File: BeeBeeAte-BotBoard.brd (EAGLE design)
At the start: 99 x 100 mm, 100 parts, among them IC1 CP2102, J1 3-1734035-2, T1 S8050, T2 S8050, U1 ESP32-WROOM-32, U2 LM5.0, U3 DRIVER 2, U4 DRIVER 1, U5 DRIVER 3, U6 DRIVER 4

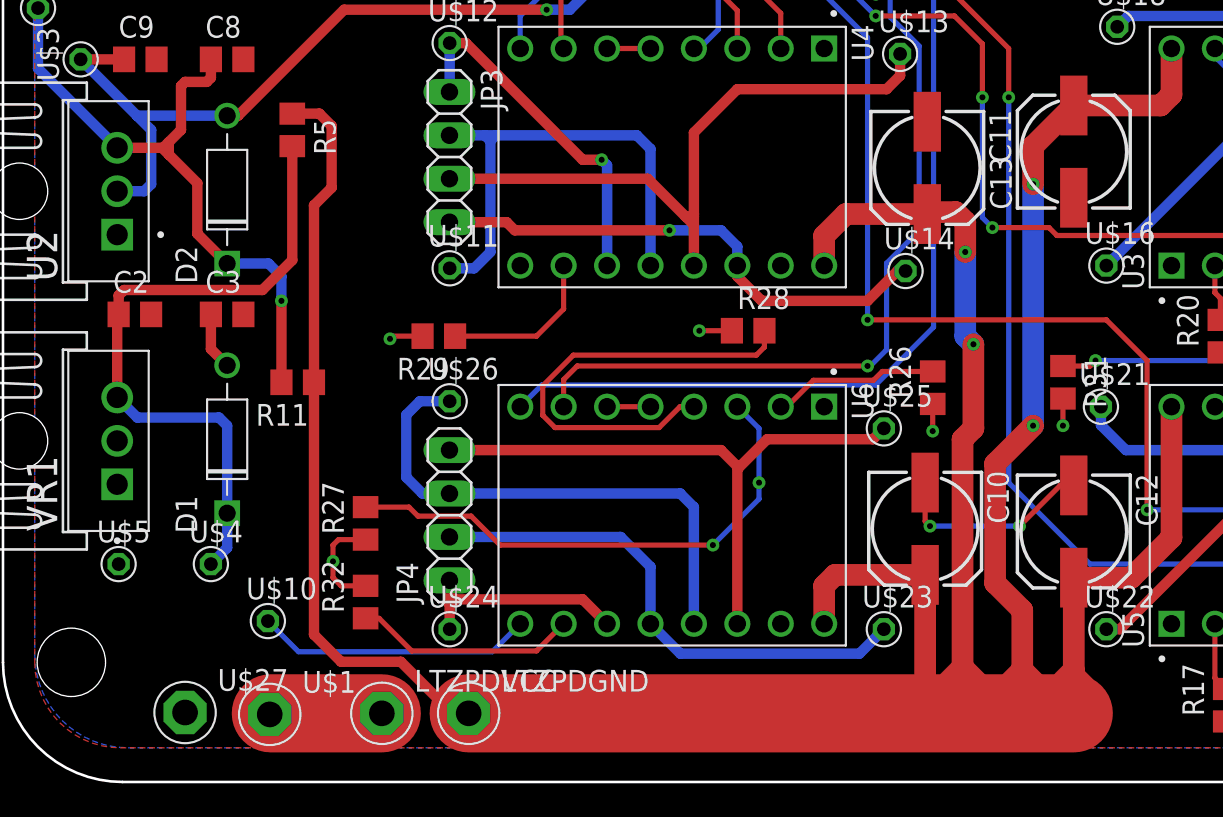
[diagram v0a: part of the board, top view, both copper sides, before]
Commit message: Added 3,7V battery
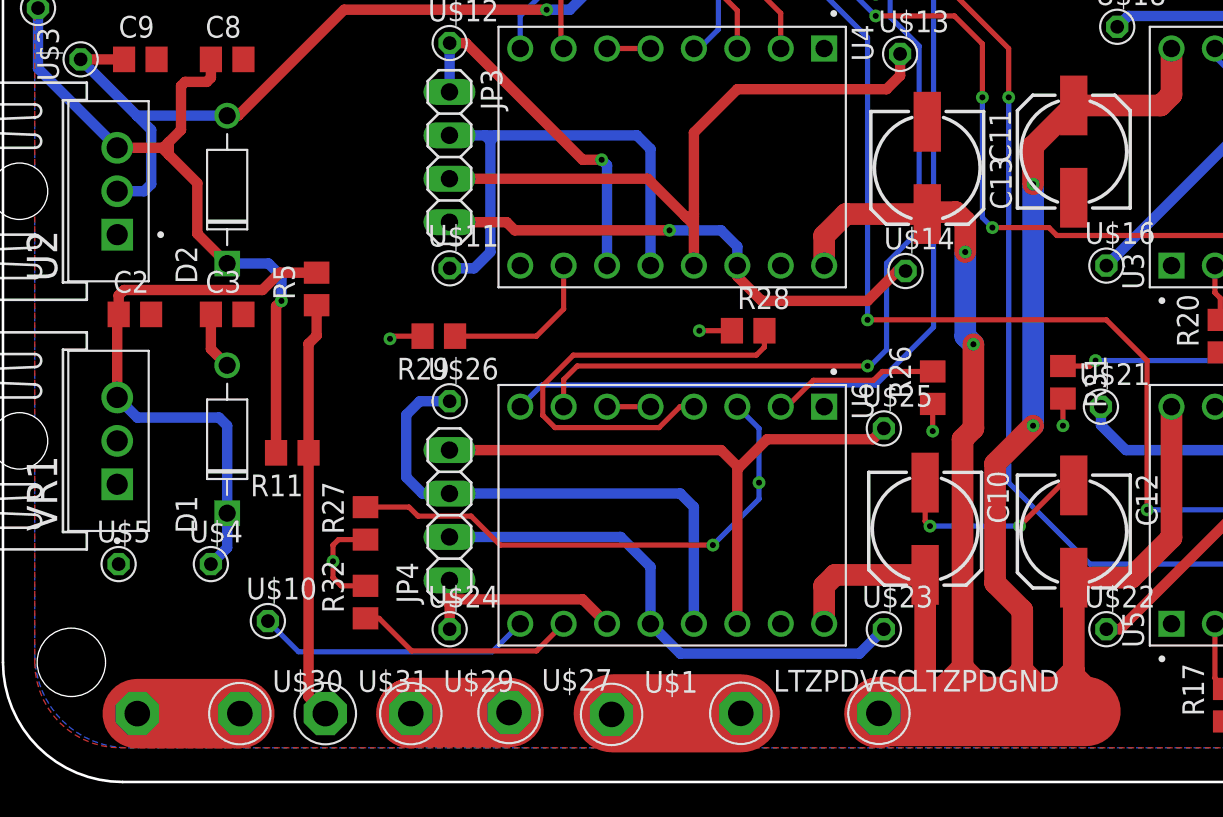
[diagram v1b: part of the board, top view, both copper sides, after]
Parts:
- added U$28: 9V+, 03lanfra-PADS:LITZENPAD
- added U$29: 9V-, 03lanfra-PADS:LITZENPAD
- added U$30: 9VSW+, 03lanfra-PADS:LITZENPAD
- added U$31: 9VSW-, 03lanfra-PADS:LITZENPAD
- moved LTZPDGND 24.0 mm to (51.4, 4.02)
- moved LTZPDVCC 21.0 mm to (43.3, 4.02)
- moved U$1 20.0 mm to (35.7, 3.95)
- moved U$27 19.0 mm to (29.7, 4.07)
- moved R5 9.41 mm to (18.5, 28.8), turned to 90 degrees
- moved R11 4.14 mm to (17.1, 19.3)
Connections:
- new net 9V: R11.1, R5.1, U$31.P$1
- new net N$15: U$28.P$1, U$30.P$1
- net GND: now also U$29.P$1
- net VCC: no longer R11.1, R5.1
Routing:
- net VCC: track 209.4 -> 142.4 mm
- net 9V: track 0.00 -> 24.5 mm
- net N$15: track 0.00 -> 6.00 mm
- net GND: track 121.6 -> 127.3 mm
- net N$4: track 39.3 -> 33.7 mm
- net N$8: track 38.6 -> 42.9 mm
- net N$5: track 6.58 -> 7.58 mm

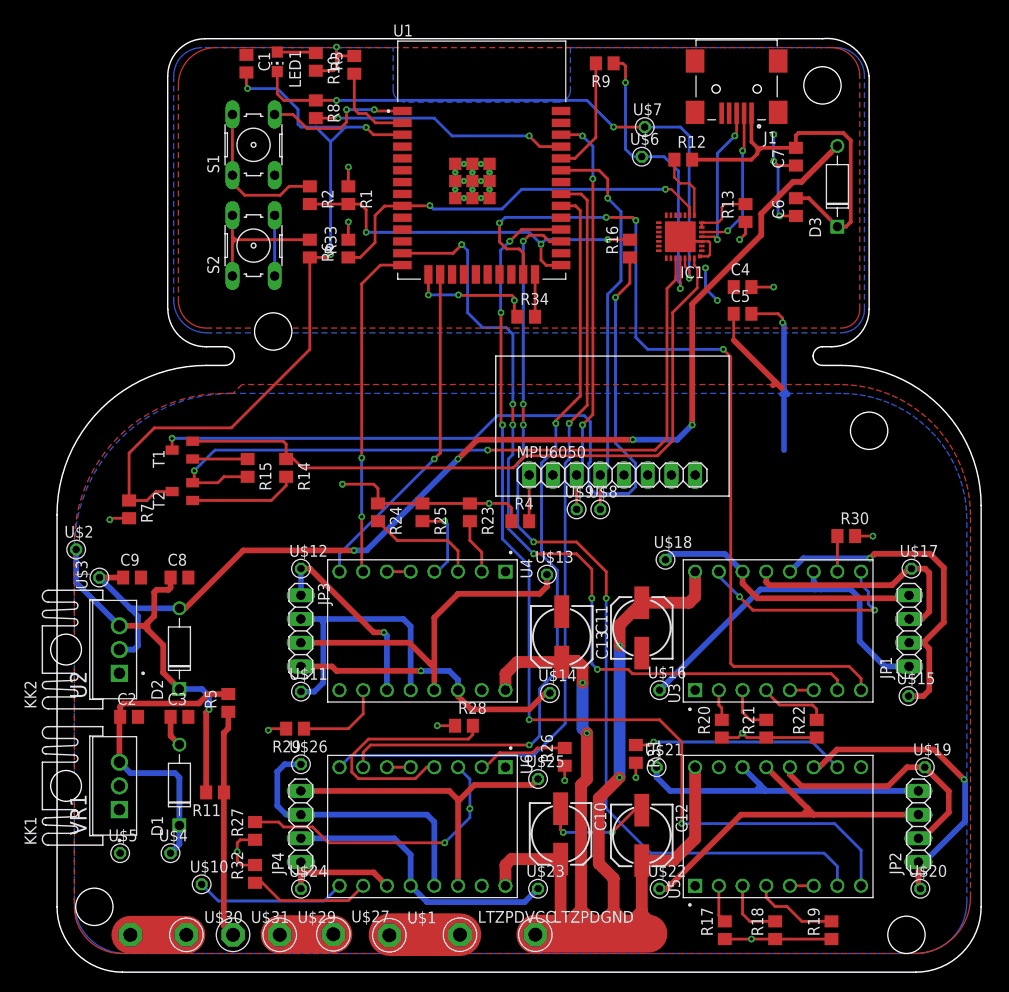
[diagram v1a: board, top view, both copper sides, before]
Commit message: Added 3D Files and modified Board
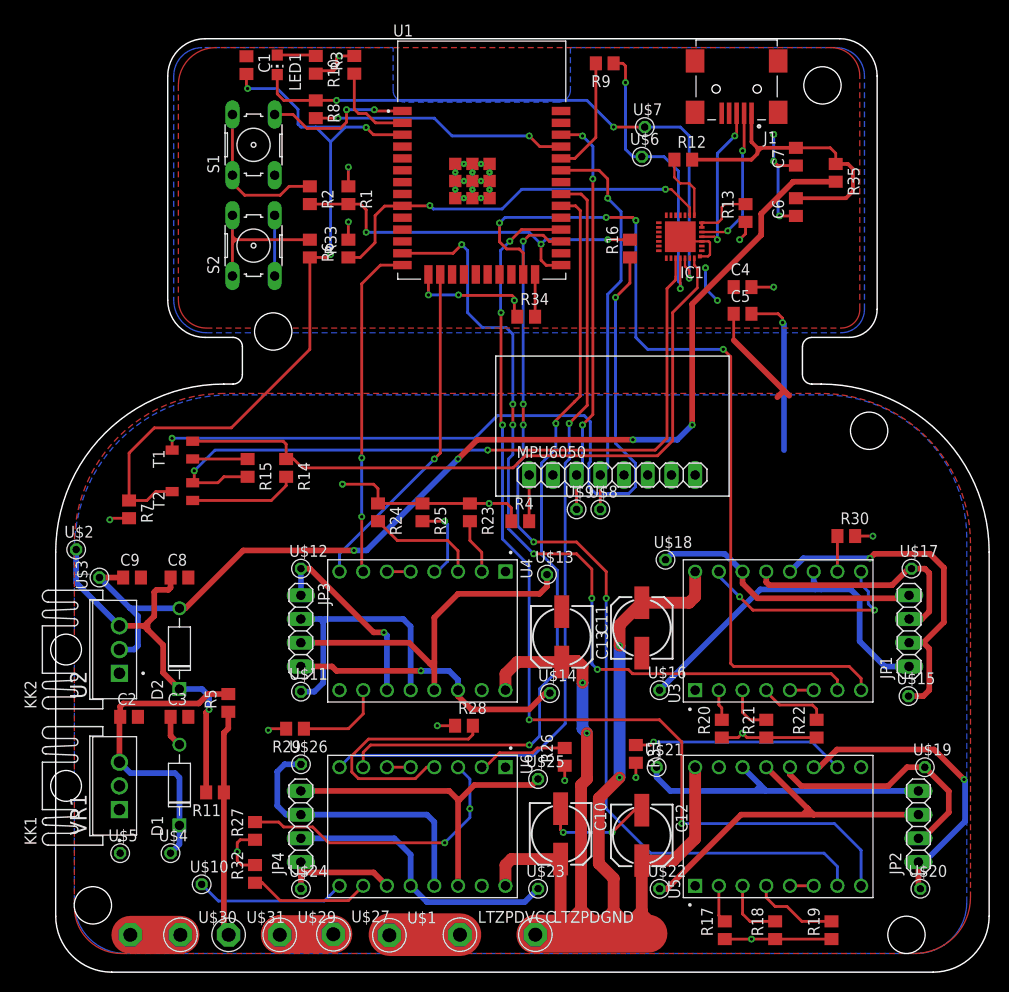
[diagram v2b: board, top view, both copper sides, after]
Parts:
- removed D3: 1N4007, Diodes:DO-41
- added R35: 0, rcl:R0805
- moved U$30 0.63 mm to (13.4, 4.00)
- moved U$31 0.48 mm to (18.5, 4.00)
- moved LED1 0.32 mm to (23.7, 97.2)
- moved R10 0.32 mm to (27.9, 97.2)
- moved C1 0.16 mm to (20.4, 97.2)
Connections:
- net 5V: now also R35.2; no longer D3.A
- net VBUS: now also R35.1; no longer D3.C
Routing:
- net VBUS: track 40.2 -> 33.0 mm
- net GND: track 127.3 -> 129.2 mm
- net 5V: track 118.9 -> 117.1 mm
- net 3V3: track 98.4 -> 96.8 mm
- net N$15: track 6.00 -> 5.37 mm
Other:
- board size 99 x 100 mm -> 100 x 100 mm
- board text added: "9V+"

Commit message: Checked by teacher and fixed
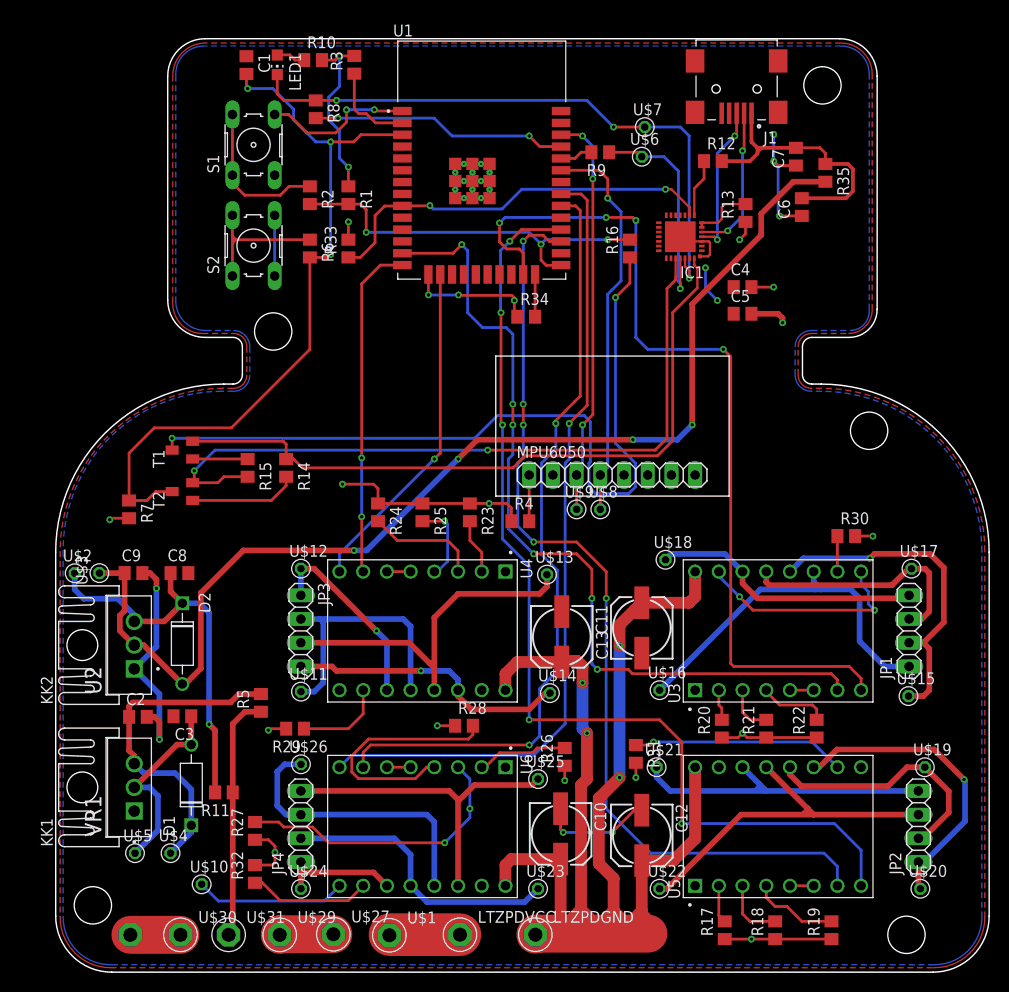
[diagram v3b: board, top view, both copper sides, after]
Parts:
- LTZPDGND: value SWITCH - -> SW-
- LTZPDVCC: value SWITCH + -> SW+
- moved R9 9.54 mm to (58.3, 87.8)
- moved R5 3.49 mm to (22.0, 28.8)
- moved R12 3.18 mm to (70.4, 86.9)
- moved U$2 2.54 mm to (2.03, 42.7)
- moved KK2 1.81 mm to (5.40, 35.0)
- moved KK1 1.75 mm to (5.40, 19.8)
- moved U2 1.66 mm to (8.41, 35.0)
- moved VR1 1.60 mm to (8.41, 19.8)
- moved U$5 1.59 mm to (8.49, 12.7)
- moved D1 1.27 mm to (14.5, 20.1)
- moved R35 1.11 mm to (82.5, 85.6)
- moved R11 0.95 mm to (18.0, 19.3)
- moved C2 0.95 mm to (8.81, 27.4)
- moved C6 0.64 mm to (79.9, 82.0)
- moved D2 0.62 mm to (13.6, 35.2), turned to 270 degrees
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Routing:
- net 3V3: track 96.8 -> 111.6 mm
- net GND: track 129.2 -> 142.3 mm, vias 14 -> 16
- net RXD: track 12.6 -> 3.52 mm
- net N$6: track 32.9 -> 24.2 mm, vias 2 -> 1
- net 5V: track 117.1 -> 123.0 mm
- net ENC: track 84.0 -> 79.9 mm
- net VBUS: track 33.0 -> 29.3 mm
- net N$4: track 33.7 -> 36.1 mm
- net 9V: track 24.3 -> 26.3 mm
- net N$11: track 7.40 -> 6.23 mm
- net N$7: track 4.17 -> 3.13 mm
